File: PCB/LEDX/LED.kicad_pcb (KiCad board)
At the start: 2 copper layers, 70 x 70 mm, 26 parts, among them J2 Conn_01x03, J3 TC2030-USB-NL-DS, P1 Square, P2 Square, P3 Square, P4 Square, U1 ICS43434_MEMS_Mic, U2 ESP32-S3-MINI-1, U5 MD8942

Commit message: Latest layout
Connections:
- J3 pad 2: DC -> D-
- J3 pad 6: GND -> D-
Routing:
- net DC: track 32.1 -> 41.4 mm, vias 4 -> 3
- net D-: track 15.6 -> 14.8 mm
- net LED1: track 25.8 -> 25.2 mm
- net GND: vias 12 -> 14

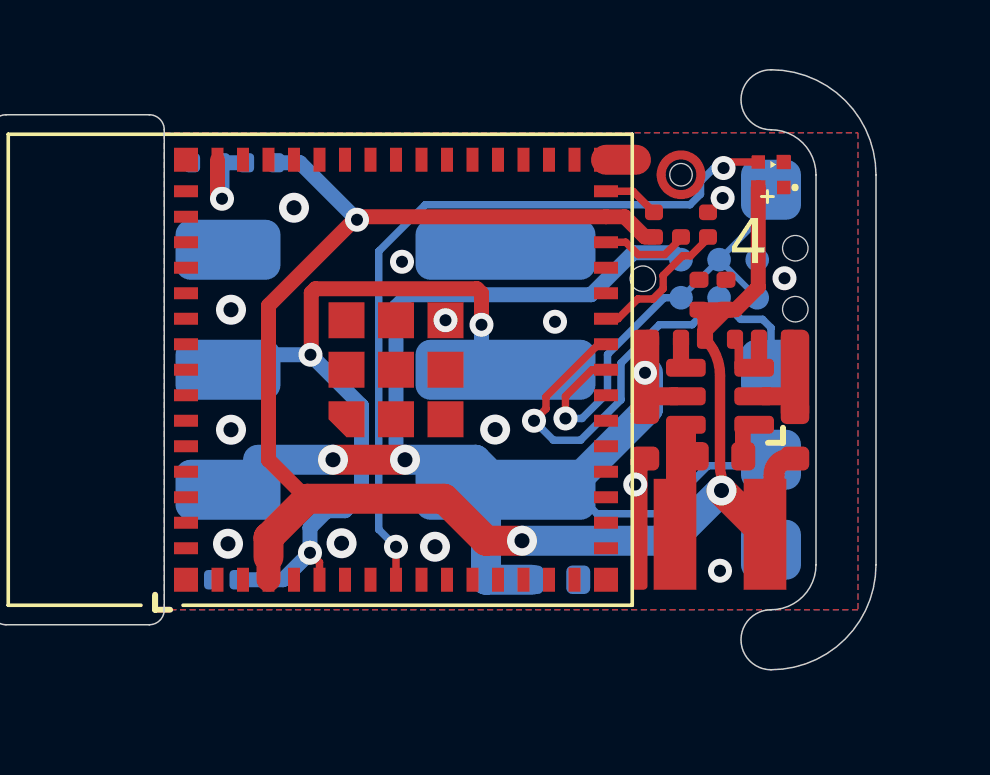
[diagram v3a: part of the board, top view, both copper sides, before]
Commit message: More caps
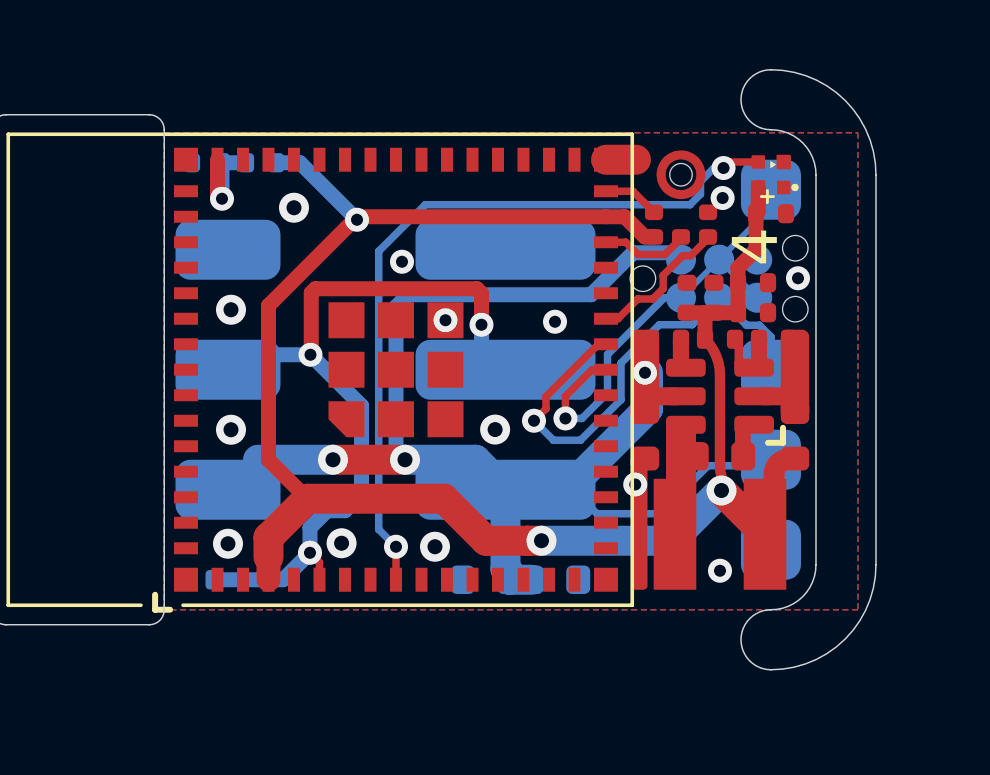
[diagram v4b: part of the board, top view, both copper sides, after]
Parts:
- added C10: 22uF, RevK:C_0402, F.Cu at (111.9, 97.1)
- added C11: 22uF, RevK:C_0402, F.Cu at (111.9, 98.1)
- added C5: 10uF 35V, RevK:C_0603, B.Cu at (103.0, 107.0)
- added C9: 22uF, RevK:C_0402, F.Cu at (112.5, 94.8)
- moved D2 0.80 mm to (93.5, 107.0)
- moved C1 0.41 mm to (110.6, 97.6)
- moved C2 0.41 mm to (109.7, 97.6)
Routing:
- net +3.3V: track 53.1 -> 52.1 mm
- net DC: track 41.4 -> 40.4 mm
- net LED1: track 25.2 -> 26.0 mm

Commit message: PCB tidy
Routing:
- net DC: track 40.4 -> 42.4 mm, vias 3 -> 4
- net GND: track 1.00 -> 2.12 mm, vias 14 -> 18

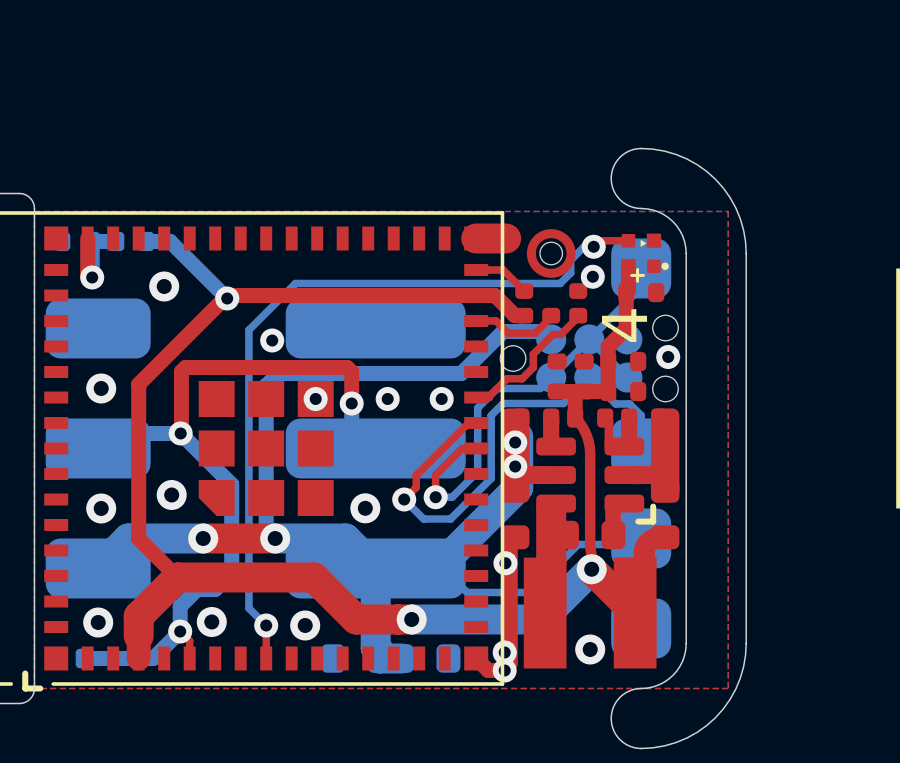
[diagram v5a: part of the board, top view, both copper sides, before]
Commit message: Changed GPIO
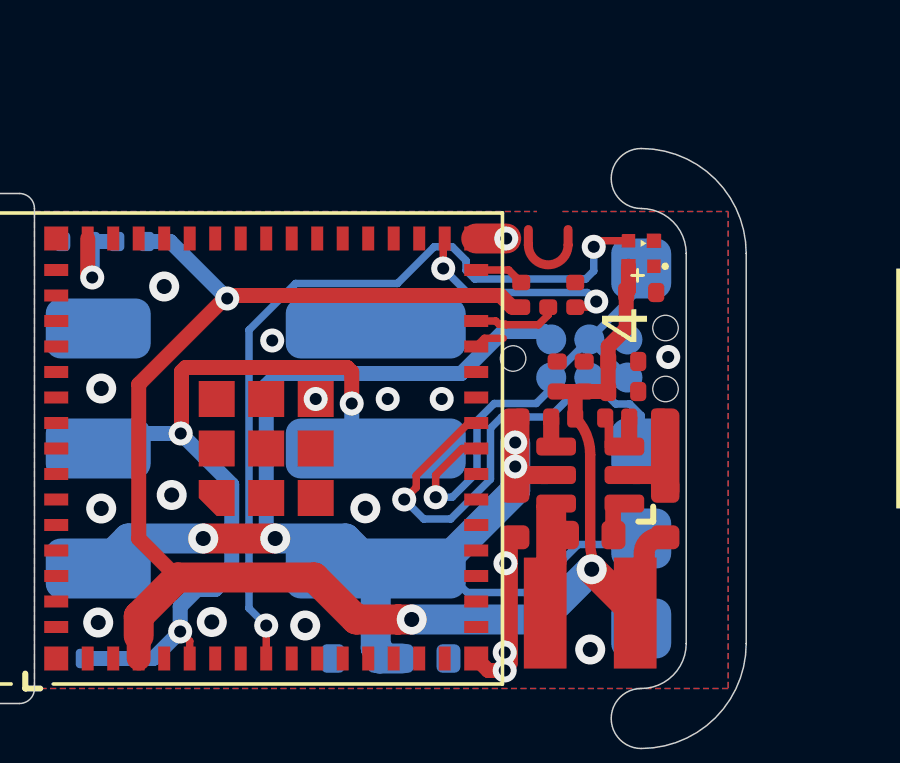
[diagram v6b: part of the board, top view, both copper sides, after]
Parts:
- U1: footprint RevK:ICS43434_MEMS_Mic -> RevK:ICS43434_MEMS_Mic_Open
- moved U1 0.30 mm to (109.4, 94.0)
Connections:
- U2 pad 25: WS -> unconnected-(U2-GPIO21-Pad25)
- U2 pad 31: unconnected-(U2-GPIO35-Pad31) -> WS
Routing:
- net WS: track 5.10 -> 7.36 mm, vias 0 -> 2
- net LED2: track 25.3 -> 26.6 mm
- net GND: track 2.12 -> 3.13 mm
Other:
- board text added: "C48 D33 W35"
- board text removed: "C48 D33 W21"

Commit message: tidy
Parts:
- U1: footprint RevK:ICS43434_MEMS_Mic_Open -> RevK:ICS43434_MEMS_Mic

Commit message: Updated (thicker case)
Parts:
- J2: footprint RevK:WAGO-2060-453-998-404 -> RevK:WAGO-2060-453-998-404-O
